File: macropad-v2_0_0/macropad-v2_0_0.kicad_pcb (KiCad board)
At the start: 2 copper layers, 13 parts, among them SW1 SW_Push, SW2 SW_Push, SW3 SW_Push, SW4 SW_Push, SW5 SW_Push, SW6 SW_Push, U1 ProMicro

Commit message: Adding README
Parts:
- added J1: Conn_01x04_Male, Connector_PinHeader_2.54mm:PinHeader_1x04_P2.54mm_Vertical, F.Cu at (94.5, 75.2)
- added SW7: Rotary_Encoder_Switch, Gauntface:ACZ11BRXE, F.Cu at (138.7, 80.8)
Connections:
- U1 pad 23: Net-(U1-Pad23) -> GND

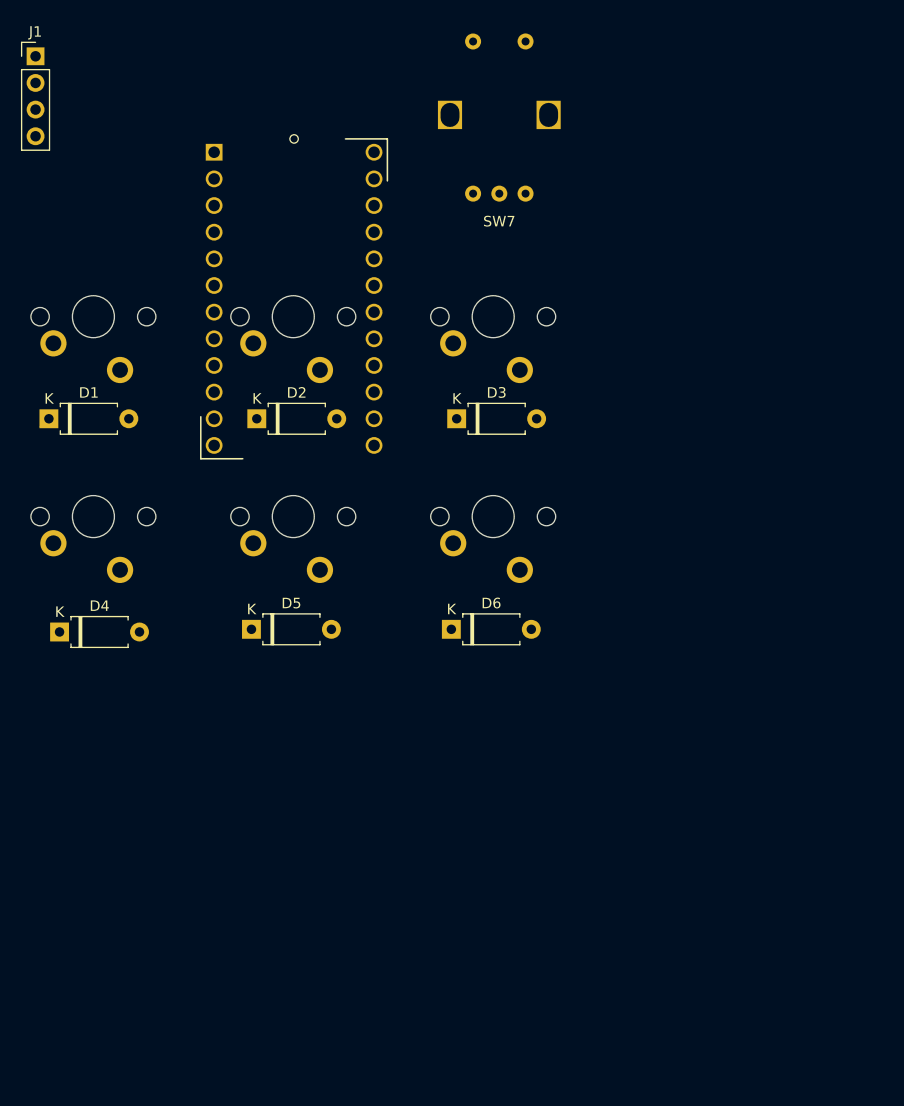
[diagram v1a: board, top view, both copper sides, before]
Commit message: Started coding up the keyboard matrix and finished v2
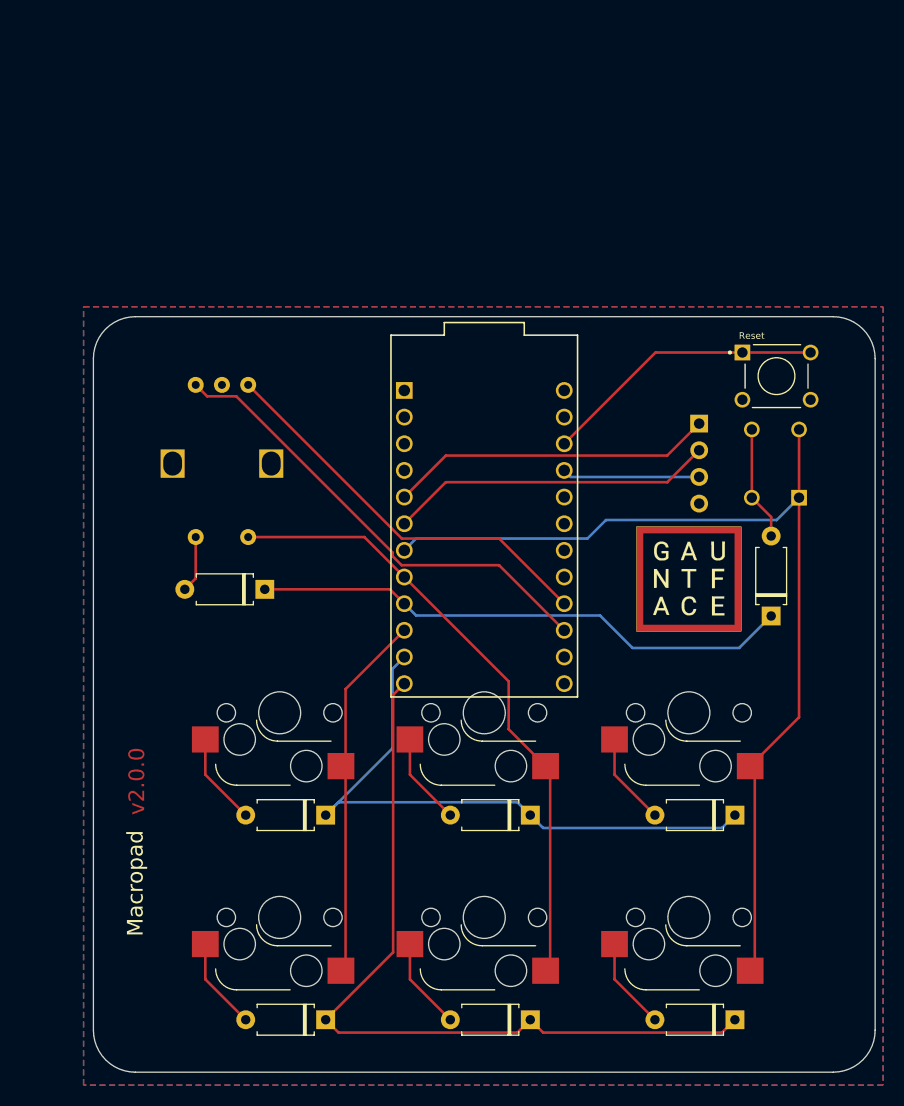
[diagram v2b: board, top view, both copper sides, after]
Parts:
- added D7: D, Diode_THT:D_A-405_P7.62mm_Horizontal, F.Cu at (116.3, 126.0)
- added D8: D, Diode_THT:D_A-405_P7.62mm_Horizontal, F.Cu at (164.6, 128.5)
- added Ref**: Val**, Gauntface:gauntface-logo, F.Cu at (156.8, 125.0)
- added Reset: Reset_Btn, Button_1825910-6:SW_1825910-6-4, F.Cu at (165.1, 105.7)
- added SW8: Layer_Btn, Button_1825910-6:SW_1825910-6-4, B.Cu at (165.0, 114.0)
- J1: footprint Connector_PinHeader_2.54mm:PinHeader_1x04_P2.54mm_Vertical -> Gauntface:Screen_38x12mm_JMD0_91_a; moved to B.Cu
- SW1: value SW_Push -> Key_1; footprint Switch_Keyboard_Cherry_MX:SW_Cherry_MX_PCB -> Switch_Keyboard_Kailh:SW_Hotswap_Kailh
- SW2: value SW_Push -> Key_2; footprint Switch_Keyboard_Cherry_MX:SW_Cherry_MX_PCB -> Switch_Keyboard_Kailh:SW_Hotswap_Kailh
- SW3: value SW_Push -> Key_3; footprint Switch_Keyboard_Cherry_MX:SW_Cherry_MX_PCB -> Switch_Keyboard_Kailh:SW_Hotswap_Kailh
- SW4: value SW_Push -> Key_4; footprint Switch_Keyboard_Cherry_MX:SW_Cherry_MX_PCB -> Switch_Keyboard_Kailh:SW_Hotswap_Kailh
- SW5: value SW_Push -> Key_5; footprint Switch_Keyboard_Cherry_MX:SW_Cherry_MX_PCB -> Switch_Keyboard_Kailh:SW_Hotswap_Kailh
- SW6: value SW_Push -> Key_6; footprint Switch_Keyboard_Cherry_MX:SW_Cherry_MX_PCB -> Switch_Keyboard_Kailh:SW_Hotswap_Kailh
- SW7: moved to B.Cu
- moved J1 59.8 mm to (140.0, 114.0), turned to 180 degrees
- moved D3 46.1 mm to (161.1, 147.5), turned to 180 degrees
- moved D1 46.1 mm to (122.1, 147.5), turned to 180 degrees
- moved D6 46.0 mm to (161.1, 167.0), turned to 180 degrees
- moved D2 45.9 mm to (141.6, 147.5), turned to 180 degrees
- moved D5 45.7 mm to (141.6, 167.0), turned to 180 degrees
- moved D4 44.8 mm to (122.1, 167.0), turned to 180 degrees
- moved SW6 42.5 mm to (156.8, 157.2)
- moved SW7 42.5 mm to (112.2, 114.0)
- moved SW5 42.3 mm to (137.2, 157.2)
- moved SW4 42.1 mm to (117.8, 157.2)
- moved SW3 42.1 mm to (156.8, 137.8)
- moved SW2 41.9 mm to (137.2, 137.8)
- moved SW1 41.7 mm to (117.8, 137.8)
- moved U1 29.0 mm to (137.2, 121.0)
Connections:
- D1 pad 1: /Row_0 -> Row_0
- D2 pad 1: /Row_0 -> Row_0
- D3 pad 1: /Row_0 -> Row_0
- D4 pad 1: /Row_1 -> Row_1
- D5 pad 1: /Row_1 -> Row_1
- D6 pad 1: /Row_1 -> Row_1
- SW1 pad 2: /Col_0 -> Col_0
- SW2 pad 2: /Col_1 -> Col_1
- SW3 pad 2: /Col_2 -> Col_2
- SW4 pad 2: /Col_0 -> Col_0
- SW5 pad 2: /Col_1 -> Col_1
- SW6 pad 2: /Col_2 -> Col_2
- SW7 pad C: Net-(SW7-PadC) -> GND
- SW7 pad S1: GND -> Encoder_S1
- SW7 pad S2: Net-(SW7-PadS2) -> Col_1
- U1 pad 10: /Col_1 -> Col_0
- U1 pad 11: /Col_2 -> Row_0
- U1 pad 12: Net-(U1-Pad12) -> Row_1
- U1 pad 15: Net-(U1-Pad15) -> Net-(SW7-PadA)
- U1 pad 16: Net-(U1-Pad16) -> Net-(SW7-PadB)
- U1 pad 17: Net-(SW7-PadS2) -> Net-(U1-Pad17)
- U1 pad 18: Net-(SW7-PadB) -> Net-(U1-Pad18)
- U1 pad 19: Net-(SW7-PadC) -> Net-(U1-Pad19)
- U1 pad 20: Net-(SW7-PadA) -> Net-(U1-Pad20)
- U1 pad 21: Net-(U1-Pad21) -> VCC
- U1 pad 3: Net-(U1-Pad3) -> GND
- U1 pad 4: Net-(U1-Pad4) -> GND
- U1 pad 7: /Row_0 -> Col_2
- U1 pad 8: /Row_1 -> Col_1
- U1 pad 9: /Col_0 -> Row_Extra
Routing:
- net Col_2: track 0.00 -> 93.6 mm
- net Row_1: track 0.00 -> 76.2 mm
- net Col_1: track 0.00 -> 59.9 mm
- net Row_0: track 0.00 -> 59.2 mm
- net Row_Extra: track 0.00 -> 51.8 mm
- net Net-(SW7-PadA): track 0.00 -> 45.0 mm
- net Net-(SW7-PadB): track 0.00 -> 38.8 mm
- net Col_0: track 0.00 -> 35.3 mm
- net Net-(J1-Pad2): track 0.00 -> 31.5 mm
- net Net-(J1-Pad1): track 0.00 -> 31.0 mm
- net Net-(SW9-Pad1): track 0.00 -> 27.1 mm
- net VCC: track 0.00 -> 13.1 mm
- net Net-(D8-Pad2): track 0.00 -> 10.9 mm
- net Net-(D6-Pad2): track 0.00 -> 8.80 mm
- net Net-(D5-Pad2): track 0.00 -> 8.80 mm
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- added copper zone on B.Cu, net GND
- added copper zone on F.Cu, net GND
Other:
- board outline added: 74.5 x 72 mm
- rule pad_to_mask_clearance: 0 -> 0.2
- rule trace_min: 0.2 -> 0.1524
- rule via_min_drill: 0.3 -> 0.254
- rule via_min_size: 0.4 -> 0.508
- board text added: "Macropad"
- board text added: "v2.0.0"
